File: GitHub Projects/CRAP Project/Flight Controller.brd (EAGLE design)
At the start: 40 x 90 mm, 107 parts, among them J1 2POS_SCREWTERM, J101 2POS_SCREWTERM, J2 4POS_SCREWTERM, J3 4POS_SCREWTERM, J4 4POS_SCREWTERM, J5 4POS_SCREWTERM, Q101 IPD042P03L3G, Q102 IPD042P03L3G

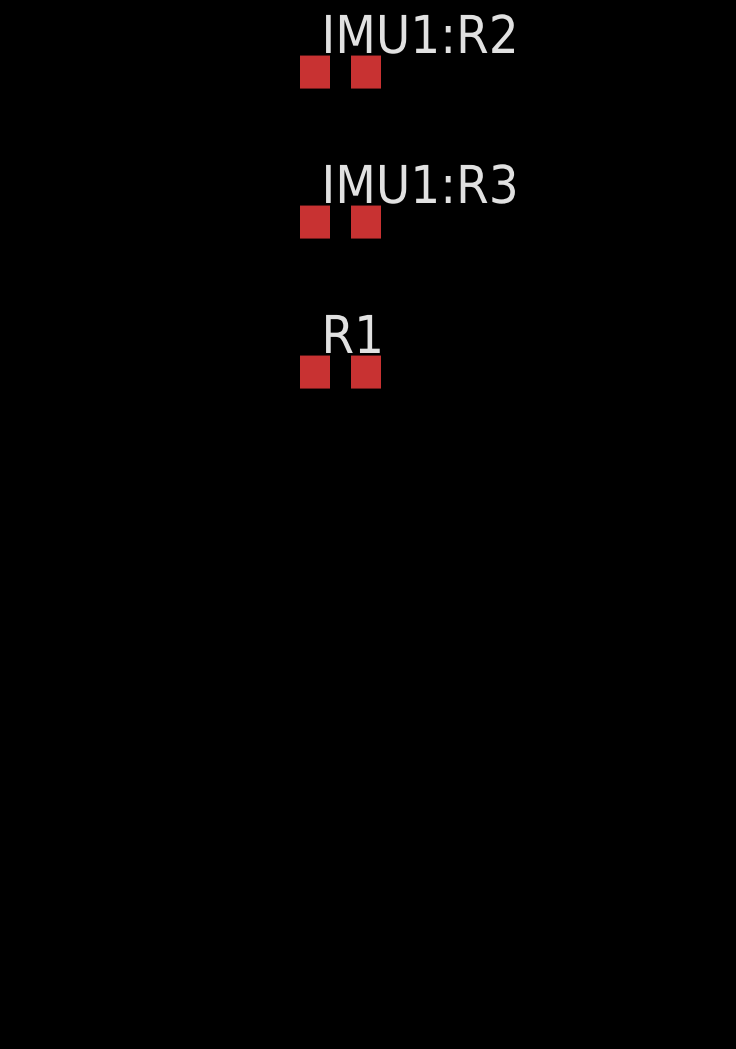
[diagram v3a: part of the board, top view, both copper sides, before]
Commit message: Added H3LIS100DL
Added the H3LIS100DL to the ST-microelectronics library along with a
3x3mm TFLGA-16 package. This device is in the HIGH_G module under
Sensors. Things for Evan to consider on this push:
1. Frame needed for the HIGH_G module schematic
2. Data communication for H3LIS100DL: SPI or I2C?
2a. If I2C, which address? Currently a resistor on the top level
schematic pulling it to 0.
3. Please check my footprint. Once again, I have more evidence for my
hate of ST: they did not provide a recommended solder footprint for the
TFLGA package. Therefore, I took the mechanical pad side of 0.35x0.25
and added 0.1 mm to each dimension to yield 0.45x0.35 (according to
their note TN0018) . I am fairly certain I centered the pads on the
pins. Yes, that is a purposeful solder mask expansion.
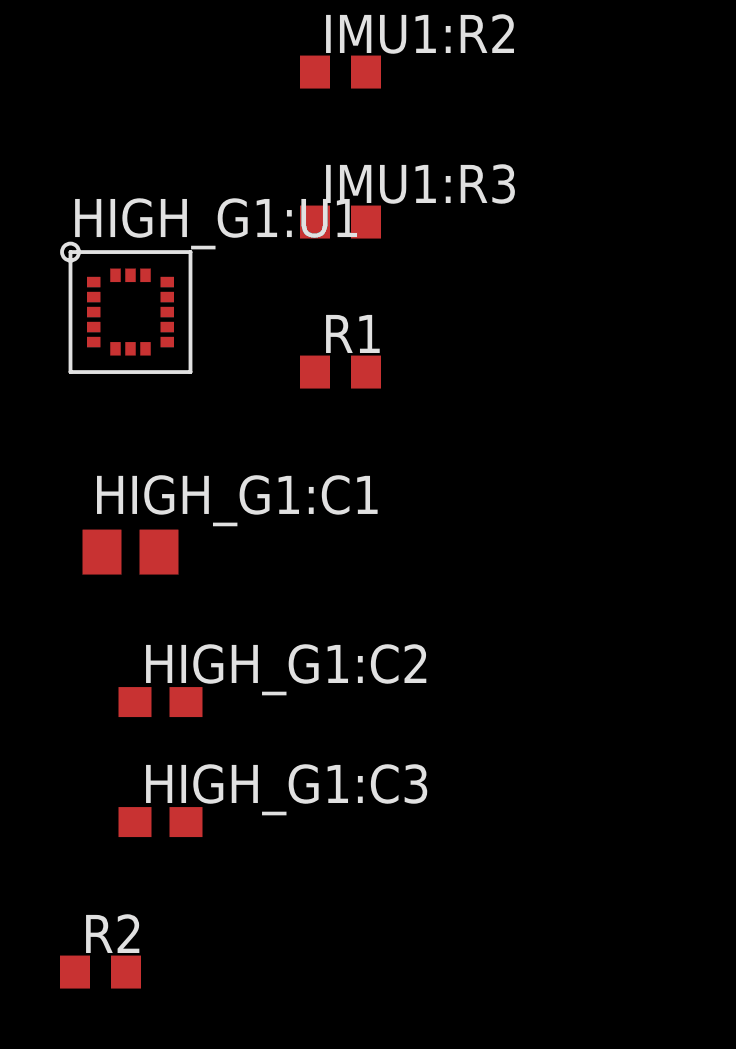
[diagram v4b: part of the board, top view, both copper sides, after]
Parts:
- added HIGH_G1:C1: 10u, rcl:C0805
- added HIGH_G1:C2, HIGH_G1:C3: 0.1u, rcl:C0603
- added HIGH_G1:U1: HDLIS100DL, st-microelectronics:TFLGA16L
- added R2: 10k, rcl:R0603
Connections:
- removed net IMU1:AD0: IMU1:U1.9
- new net HIGH_G1:CS: HIGH_G1:U1.P8
- new net HIGH_G1:INT1: HIGH_G1:U1.P11
- new net HIGH_G1:INT2: HIGH_G1:U1.P9
- new net HIGH_G1:SCL/SPC: HIGH_G1:U1.P4
- new net HIGH_G1:SDA/SDI: HIGH_G1:U1.P6
- new net N$14: IMU1:U1.9, R1.2
- new net N$15: HIGH_G1:U1.P7, R2.2
- net +3V3: now also HIGH_G1:C1.1, HIGH_G1:C2.1, HIGH_G1:C3.1, HIGH_G1:U1.P1, HIGH_G1:U1.P14, HIGH_G1:U1.P15
- net GND: now also HIGH_G1:C1.2, HIGH_G1:C2.2, HIGH_G1:C3.2, HIGH_G1:U1.P10, HIGH_G1:U1.P12, HIGH_G1:U1.P13, HIGH_G1:U1.P16, HIGH_G1:U1.P5, R1.1, R2.1
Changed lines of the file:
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@@
 <element name="IMU1:R3" library="rcl" package="R0603" value="2.2K" x="-112" y="-135"/>
 <element name="R1" library="rcl" package="R0603" value="10k" x="-112" y="-140"/>
+<element name="HIGH_G1:U1" library="st-microelectronics" package="TFLGA16L" value="HDLIS100DL" x="-119" y="-138"/>
+<element name="HIGH_G1:C1" library="rcl" package="C0805" value="10u" x="-119" y="-146"/>
+<element name="HIGH_G1:C2" library="rcl" package="C0603" value="0.1u" x="-118" y="-151"/>
+<element name="HIGH_G1:C3" library="rcl" package="C0603" value="0.1u" x="-118" y="-155"/>
+<element name="R2" library="rcl" package="R0603" value="10k" x="-120" y="-160"/>
 </elements>
 <signals>
@@
 <contactref element="IMU1:C2" pad="2"/>
 <contactref element="IMU1:C1" pad="2"/>
+<contactref element="R1" pad="1"/>
+<contactref element="R2" pad="1"/>
+<contactref element="HIGH_G1:U1" pad="P10"/>
+<contactref element="HIGH_G1:U1" pad="P12"/>
+<contactref element="HIGH_G1:U1" pad="P5"/>
+<contactref element="HIGH_G1:U1" pad="P16"/>
+<contactref element="HIGH_G1:U1" pad="P13"/>
+<contactref element="HIGH_G1:C2" pad="2"/>
+<contactref element="HIGH_G1:C1" pad="2"/>
+<contactref element="HIGH_G1:C3" pad="2"/>
+<wire x1="-117.775" y1="-138.5" x2="-112.85" y2="-140" width="0" layer="19" extent="1-1"/>
+<wire x1="-117.775" y1="-137.5" x2="-117.775" y2="-138.5" width="0" layer="19" extent="1-1"/>
+<wire x1="-117.775" y1="-137" x2="-117.775" y2="-137.5" width="0" layer="19" extent="1-1"/>
+<wire x1="-119.5" y1="-136.775" x2="-117.775" y2="-137" width="0" layer="19" extent="1-1"/>
+<wire x1="-120.225" y1="-139" x2="-119.5" y2="-136.775" width="0" layer="19" extent="1-1"/>
+<wire x1="-118.05" y1="-146" x2="-120.225" y2="-139" width="0" layer="19" extent="1-1"/>
+<wire x1="-117.15" y1="-151" x2="-118.05" y2="-146" width="0" layer="19" extent="1-1"/>
+<wire x1="-117.15" y1="-155" x2="-117.15" y2="-151" width="0" layer="19" extent="1-1"/>
+<wire x1="-120.85" y1="-160" x2="-117.15" y2="-155" width="0" layer="19" extent="1-1"/>
+<wire x1="-109.15" y1="-120" x2="-117.775" y2="-137" width="0" layer="19" extent="1-1"/>
 <wire x1="-109.15" y1="-116" x2="-109.15" y2="-120" width="0" layer="19" extent="1-1"/>
 <wire x1="-109.15" y1="-112" x2="-109.15" y2="-116" width="0" layer="19" extent="1-1"/>
@@
 <contactref element="IMU1:R2" pad="2"/>
 <contactref element="IMU1:R3" pad="2"/>
+<contactref element="HIGH_G1:U1" pad="P14"/>
+<contactref element="HIGH_G1:U1" pad="P1"/>
+<contactref element="HIGH_G1:U1" pad="P15"/>
+<contactref element="HIGH_G1:C1" pad="1"/>
+<contactref element="HIGH_G1:C2" pad="1"/>
+<contactref element="HIGH_G1:C3" pad="1"/>
+<wire x1="-119" y1="-136.775" x2="-118.5" y2="-136.775" width="0" layer="19" extent="1-1"/>
+<wire x1="-120.225" y1="-137" x2="-119" y2="-136.775" width="0" layer="19" extent="1-1"/>
+<wire x1="-111.15" y1="-135" x2="-118.5" y2="-136.775" width="0" layer="19" extent="1-1"/>
 <wire x1="-111.15" y1="-130" x2="-111.15" y2="-135" width="0" layer="19" extent="1-1"/>
+<wire x1="-119.95" y1="-146" x2="-120.225" y2="-137" width="0" layer="19" extent="1-1"/>
+<wire x1="-118.85" y1="-151" x2="-119.95" y2="-146" width="0" layer="19" extent="1-1"/>
+<wire x1="-118.85" y1="-155" x2="-118.85" y2="-151" width="0" layer="19" extent="1-1"/>
 <wire x1="-110.85" y1="-120" x2="-111.15" y2="-130" width="0" layer="19" extent="1-1"/>
 <wire x1="-111.15" y1="-18" x2="-110.85" y2="-120" width="0" layer="19" extent="1-1"/>
@@
 <wire x1="-99.19" y1="-1.54" x2="-98.39" y2="-3.94" width="0" layer="19" extent="1-1"/>
 </signal>
-<signal name="IMU1:AD0">
-<contactref element="IMU1:U1" pad="9"/>
-</signal>
 <signal name="IMU1:INT">
 <contactref element="IMU1:U1" pad="12"/>
 </signal>
+<signal name="N$14">
+<contactref element="R1" pad="2"/>
+<contactref element="IMU1:U1" pad="9"/>
+<wire x1="-97.99" y1="-3.94" x2="-111.15" y2="-140" width="0" layer="19" extent="1-1"/>
+</signal>
+<signal name="HIGH_G1:INT2">
+<contactref element="HIGH_G1:U1" pad="P9"/>
+</signal>
+<signal name="HIGH_G1:INT1">
+<contactref element="HIGH_G1:U1" pad="P11"/>
+</signal>
+<signal name="HIGH_G1:CS">
+<contactref element="HIGH_G1:U1" pad="P8"/>
+</signal>
+<signal name="HIGH_G1:SDA/SDI">
+<contactref element="HIGH_G1:U1" pad="P6"/>
+</signal>
+<signal name="HIGH_G1:SCL/SPC">
+<contactref element="HIGH_G1:U1" pad="P4"/>
+</signal>
+<signal name="N$15">
+<contactref element="HIGH_G1:U1" pad="P7"/>
+<contactref element="R2" pad="2"/>
+<wire x1="-119" y1="-139.225" x2="-119.15" y2="-160" width="0" layer="19" extent="1-1"/>
+</signal>
 </signals>

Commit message: Ordnance power updates
1. Fixed PGOOD LED on Ordnance Power module
2. Wired output capacitors on Ordnance Power. This is a single super-cap
configuration where two 100uF caps in series are needed fro the
balancing circuitry.
3. Added a frame to the HIGH_G module

Another issue discovered:
1. Need USB connection. There are no micro USBs in the library (unless
I'm blind?)
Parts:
- removed R304: 10k, resistor:R0603
- added C306, C307: 100u, rcl:C1206
- added D302: LTST-C193KRKT-2A, led:CHIP-LED0603
- C304: value 1u -> 0.1u
- R302: value 100k -> 2.2k
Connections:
- removed net ORDNANCE_POWER:N$10: U301.P3
- removed net ORDNANCE_POWER:N$8: C304.1, R302.1, R304.2, U301.P5
- new net ORDNANCE_POWER:N$4: C304.1, D302.A, R302.1, U301.P5
- new net ORDNANCE_POWER:N$7: C306.2, C307.1, U301.P3
- net +3V3: now also R302.2
- net GND: now also C307.2, D302.C
- net ORDNANCE_POWER:N$3: now also C306.1
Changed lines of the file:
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@@
 <element name="C302" library="rcl" package="C0805" value="1u" x="-49.53" y="176.53"/>
 <element name="C303" library="rcl" package="C0603" value="1u" x="-87.63" y="175.26"/>
-<element name="C304" library="rcl" package="C0603" value="1u" x="-93.98" y="175.26"/>
+<element name="C304" library="rcl" package="C0603" value="0.1u" x="-93.98" y="175.26"/>
 <element name="C401" library="rcl" package="C0603" value="0.1 u" x="-34.29" y="203.2"/>
 <element name="C402" library="rcl" package="C0603" value="0.1 u" x="-40.64" y="203.2"/>
@@
 <element name="R106" library="rcl" package="R0603" value="10k" x="-55.88" y="167.64"/>
 <element name="R301" library="resistor" package="R0603" value="10k" x="-62.23" y="175.26"/>
-<element name="R302" library="resistor" package="R0603" value="100k" x="-68.58" y="175.26"/>
+<element name="R302" library="resistor" package="R0603" value="2.2k" x="-68.58" y="175.26"/>
 <element name="R303" library="resistor" package="R0603" value="12k" x="-74.93" y="175.26"/>
-<element name="R304" library="resistor" package="R0603" value="10k" x="-81.28" y="175.26"/>
 <element name="R401" library="rcl" package="R0603" value="1.2 k" x="-46.99" y="203.2"/>
 <element name="R402" library="rcl" package="R0603" value="1.2 k" x="-53.34" y="203.2"/>
@@
 <element name="HIGH_G1:C3" library="rcl" package="C0603" value="0.1u" x="-118" y="-155"/>
 <element name="R2" library="rcl" package="R0603" value="10k" x="-120" y="-160"/>
+<element name="D302" library="led" package="CHIP-LED0603" value="LTST-C193KRKT-2A" x="-124" y="-161"/>
+<element name="C306" library="rcl" package="C1206" value="100u" x="-123" y="-166"/>
+<element name="C307" library="rcl" package="C1206" value="100u" x="-123" y="-172"/>
 </elements>
 <signals>
@@
 <contactref element="HIGH_G1:C1" pad="2"/>
 <contactref element="HIGH_G1:C3" pad="2"/>
+<contactref element="D302" pad="C"/>
+<contactref element="C307" pad="2"/>
 <wire x1="-117.775" y1="-138.5" x2="-112.85" y2="-140" width="0" layer="19" extent="1-1"/>
 <wire x1="-117.775" y1="-137.5" x2="-117.775" y2="-138.5" width="0" layer="19" extent="1-1"/>
@@
 <wire x1="-117.15" y1="-155" x2="-117.15" y2="-151" width="0" layer="19" extent="1-1"/>
 <wire x1="-120.85" y1="-160" x2="-117.15" y2="-155" width="0" layer="19" extent="1-1"/>
+<wire x1="-124" y1="-160.25" x2="-120.85" y2="-160" width="0" layer="19" extent="1-1"/>
+<wire x1="-121.6" y1="-172" x2="-124" y2="-160.25" width="0" layer="19" extent="1-1"/>
 <wire x1="-109.15" y1="-120" x2="-117.775" y2="-137" width="0" layer="19" extent="1-1"/>
 <wire x1="-109.15" y1="-116" x2="-109.15" y2="-120" width="0" layer="19" extent="1-1"/>
@@
 <contactref element="HIGH_G1:C2" pad="1"/>
 <contactref element="HIGH_G1:C3" pad="1"/>
+<contactref element="R302" pad="2"/>
 <wire x1="-119" y1="-136.775" x2="-118.5" y2="-136.775" width="0" layer="19" extent="1-1"/>
 <wire x1="-120.225" y1="-137" x2="-119" y2="-136.775" width="0" layer="19" extent="1-1"/>
@@
 <wire x1="-56.11" y1="175.26" x2="-48.68" y2="167.64" width="0" layer="19" extent="1-1"/>
 <wire x1="-61.38" y1="175.26" x2="-56.11" y2="175.26" width="0" layer="19" extent="1-1"/>
-<wire x1="-75.78" y1="167.64" x2="-61.38" y2="175.26" width="0" layer="19" extent="1-1"/>
+<wire x1="-67.73" y1="175.26" x2="-61.38" y2="175.26" width="0" layer="19" extent="1-1"/>
+<wire x1="-75.78" y1="167.64" x2="-67.73" y2="175.26" width="0" layer="19" extent="1-1"/>
 <wire x1="-88.48" y1="175.26" x2="-75.78" y2="167.64" width="0" layer="19" extent="1-1"/>
 <wire x1="-78.42" y1="152.4" x2="-75.78" y2="167.64" width="0" layer="19" extent="1-1"/>
@@
 <wire x1="-74.08" y1="175.26" x2="-55.11" y2="175.26" width="0" layer="19" extent="1-1"/>
 </signal>
-<signal name="ORDNANCE_POWER:N$10">
-<contactref element="U301" pad="P3"/>
-</signal>
-<signal name="ORDNANCE_POWER:N$8">
-<contactref element="R304" pad="2"/>
-<contactref element="U301" pad="P5"/>
-<contactref element="R302" pad="1"/>
-<contactref element="C304" pad="1"/>
-<wire x1="-69.43" y1="175.26" x2="-54.61" y2="173.41" width="0" layer="19" extent="1-1"/>
-<wire x1="-80.43" y1="175.26" x2="-69.43" y2="175.26" width="0" layer="19" extent="1-1"/>
-<wire x1="-94.83" y1="175.26" x2="-80.43" y2="175.26" width="0" layer="19" extent="1-1"/>
-</signal>
 <signal name="+12V">
 <contactref element="D301" pad="3"/>
@@
 <contactref element="U301" pad="P10"/>
 <contactref element="C305" pad="1"/>
+<contactref element="C306" pad="1"/>
 <wire x1="-36.57" y1="175.54" x2="-32.01" y2="175.54" width="0" layer="19" extent="1-1"/>
 <wire x1="-56.61" y1="175.26" x2="-36.57" y2="175.54" width="0" layer="19" extent="1-1"/>
-<wire x1="24" y1="71.25" x2="-56.61" y2="175.26" width="0" layer="19" extent="1-1"/>
+<wire x1="24" y1="71.25" x2="-32.01" y2="175.54" width="0" layer="19" extent="1-1"/>
+<wire x1="-124.4" y1="-166" x2="24" y2="71.25" width="0" layer="19" extent="1-1"/>
 </signal>
 <signal name="FC4+">
@@
 <wire x1="-119" y1="-139.225" x2="-119.15" y2="-160" width="0" layer="19" extent="1-1"/>
 </signal>
+<signal name="ORDNANCE_POWER:N$4">
+<contactref element="D302" pad="A"/>
+<contactref element="R302" pad="1"/>
+<contactref element="U301" pad="P5"/>
+<contactref element="C304" pad="1"/>
+<wire x1="-69.43" y1="175.26" x2="-54.61" y2="173.41" width="0" layer="19" extent="1-1"/>
+<wire x1="-94.83" y1="175.26" x2="-69.43" y2="175.26" width="0" layer="19" extent="1-1"/>
+<wire x1="-124" y1="-161.75" x2="-94.83" y2="175.26" width="0" layer="19" extent="1-1"/>
+</signal>
+<signal name="ORDNANCE_POWER:N$7">
+<contactref element="C306" pad="2"/>
+<contactref element="C307" pad="1"/>
+<contactref element="U301" pad="P3"/>
+<wire x1="-121.6" y1="-166" x2="-55.61" y2="173.41" width="0" layer="19" extent="1-1"/>
+<wire x1="-124.4" y1="-172" x2="-121.6" y2="-166" width="0" layer="19" extent="1-1"/>
+</signal>
 </signals>

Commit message: Ordnance & Breakwire modules fixes
1. In the Ordnance module: combined the PYRO+ and PWR to the same pin
and called PWR/PYRO+. This is the ordnance power from the super caps.
2. In the Ordnance module: combined CONT_STAT and PYRO– to the same pin
and called CONT_STAT/PYRO–. Outside the modules on the top level
schematic, I added long wires from this pin going to the left of each
module. This is also the digital line for sensing continuity status of
the ordnance lines.
3. In the Breakwire module, combined BW_STAT and BW– to the same pin and
called BW_STAT/BW–. Outside the module on the top level schematic, I
made long lines from this pin to the right of each module. This is the
digital input for sensing the breakwire status (open or closed).
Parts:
- C104: value 100n -> 2.2 u
- R101: value (none) -> 100k
- R102: value (none) -> 1k
- moved FIRING_CIRCUIT4:R4 489.1 mm to (-124.0, -334.0)
- moved FIRING_CIRCUIT4:R3 454.4 mm to (-124.0, -329.0)
- moved FIRING_CIRCUIT4:R2 451.8 mm to (-124.0, -324.0)
- moved FIRING_CIRCUIT4:R1 450.0 mm to (-124.0, -319.0)
- moved FIRING_CIRCUIT4:Q2 443.9 mm to (-121.0, -306.0)
- moved FIRING_CIRCUIT4:Q1 441.7 mm to (-115.0, -292.0)
- moved FIRING_CIRCUIT3:R4 406.0 mm to (-124.0, -277.0)
- moved FIRING_CIRCUIT3:R3 370.0 mm to (-124.0, -272.0)
- moved FIRING_CIRCUIT3:R2 367.9 mm to (-124.0, -267.0)
- moved FIRING_CIRCUIT3:R1 366.8 mm to (-124.0, -262.0)
- moved FIRING_CIRCUIT3:Q2 361.8 mm to (-121.0, -249.0)
- moved FIRING_CIRCUIT3:Q1 357.9 mm to (-115.0, -235.0)
- moved FIRING_CIRCUIT2:R4 324.0 mm to (-124.0, -220.0)
- moved FIRING_CIRCUIT4:D1 287.3 mm to (-125.0, -344.0)
- moved FIRING_CIRCUIT2:R3 285.9 mm to (-124.0, -215.0)
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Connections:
- net FC2- renamed FC1-1
- net FC4- renamed FC1-3
- removed net FC1+: FIRING_CIRCUIT1:R1.1, FIRING_CIRCUIT1:R5.2, J3.1
- removed net FC3+: FIRING_CIRCUIT3:R1.1, FIRING_CIRCUIT3:R5.2, J4.1
- removed net FIRING_CIRCUIT1:+3V3: FIRING_CIRCUIT1:Q1.3, FIRING_CIRCUIT1:R4.2
- removed net FIRING_CIRCUIT2:+3V3: FIRING_CIRCUIT2:Q1.3, FIRING_CIRCUIT2:R4.2
- removed net FIRING_CIRCUIT3:+3V3: FIRING_CIRCUIT3:Q1.3, FIRING_CIRCUIT3:R4.2
- removed net FIRING_CIRCUIT4:+3V3: FIRING_CIRCUIT4:Q1.3, FIRING_CIRCUIT4:R4.2
- new net BREAKWIRE2:BW_STAT/BW–: BREAKWIRE2:C1.1
- new net FC1-2: FIRING_CIRCUIT3:C1.1, FIRING_CIRCUIT3:Q2.7, FIRING_CIRCUIT3:Q2.8, FIRING_CIRCUIT3:R5.1
- net +12V: now also FIRING_CIRCUIT1:R1.1, FIRING_CIRCUIT1:R5.2, FIRING_CIRCUIT2:R1.1, FIRING_CIRCUIT2:R5.2, FIRING_CIRCUIT3:R1.1, FIRING_CIRCUIT3:R5.2, FIRING_CIRCUIT4:R1.1, FIRING_CIRCUIT4:R5.2, J3.1, J4.1
- net +3V3: now also FIRING_CIRCUIT1:Q1.3, FIRING_CIRCUIT1:R4.2, FIRING_CIRCUIT2:Q1.3, FIRING_CIRCUIT2:R4.2, FIRING_CIRCUIT3:Q1.3, FIRING_CIRCUIT3:R4.2, FIRING_CIRCUIT4:Q1.3, FIRING_CIRCUIT4:R4.2
- net FC2+: no longer FIRING_CIRCUIT2:R1.1, FIRING_CIRCUIT2:R5.2
- net FC3-: no longer FIRING_CIRCUIT3:C1.1, FIRING_CIRCUIT3:Q2.7, FIRING_CIRCUIT3:Q2.8, FIRING_CIRCUIT3:R5.1
- net FC4+: no longer FIRING_CIRCUIT4:R1.1, FIRING_CIRCUIT4:R5.2
- net N$12: no longer BREAKWIRE2:C1.1
